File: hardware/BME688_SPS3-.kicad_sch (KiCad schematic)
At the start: 6 parts, among them U59 USBLC6-2P6, U6 BME688

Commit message: updated annotations
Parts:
- renumbered C25 to C501, C12 to C502, D11 to D501, SPS30_Connector4 to SPS30_Connector501, U6 to U501, U59 to U502
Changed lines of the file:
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@@
 		(dnp no)
 		(fields_autoplaced yes)
-		(property "Reference" "#PWR026"
+		(property "Reference" "#PWR0502"
 			(at 121.92 132.08 0)
 			(effects
@@
 			(project "Senior_Design"
 				(path "/8f5928e8-0fc1-4443-a20f-3bfeb956761e/140ad835-eaa4-4a8c-a4e7-0525bbf22a2e"
-					(reference "#PWR026")
+					(reference "#PWR0502")
 					(unit 1)
 				)
@@
 		(dnp no)
 		(fields_autoplaced yes)
-		(property "Reference" "#PWR077"
+		(property "Reference" "#PWR0501"
 			(at 87.63 111.76 0)
 			(effects
@@
 			(project "Senior_Design"
 				(path "/8f5928e8-0fc1-4443-a20f-3bfeb956761e/140ad835-eaa4-4a8c-a4e7-0525bbf22a2e"
-					(reference "#PWR077")
+					(reference "#PWR0501")
 					(unit 1)
 				)
@@
 		(on_board yes)
 		(dnp no)
-		(property "Reference" "C12"
+		(property "Reference" "C502"
 			(at 136.398 119.888 0)
 			(effects
@@
 			(project "Senior_Design"
 				(path "/8f5928e8-0fc1-4443-a20f-3bfeb956761e/140ad835-eaa4-4a8c-a4e7-0525bbf22a2e"
-					(reference "C12")
+					(reference "C502")
 					(unit 1)
 				)
@@
 		(dnp no)
 		(fields_autoplaced yes)
-		(property "Reference" "U59"
+		(property "Reference" "U502"
 			(at 141.3511 60.96 0)
 			(effects
@@
 			(project "Senior_Design"
 				(path "/8f5928e8-0fc1-4443-a20f-3bfeb956761e/140ad835-eaa4-4a8c-a4e7-0525bbf22a2e"
-					(reference "U59")
+					(reference "U502")
 					(unit 1)
 				)
@@
 		(dnp no)
 		(fields_autoplaced yes)
-		(property "Reference" "#PWR078"
+		(property "Reference" "#PWR0503"
 			(at 139.7 67.31 0)
 			(effects
@@
 			(project "Senior_Design"
 				(path "/8f5928e8-0fc1-4443-a20f-3bfeb956761e/140ad835-eaa4-4a8c-a4e7-0525bbf22a2e"
-					(reference "#PWR078")
+					(reference "#PWR0503")
 					(unit 1)
 				)
@@
 		(dnp no)
 		(fields_autoplaced yes)
-		(property "Reference" "U6"
+		(property "Reference" "U501"
 			(at 102.87 96.52 0)
 			(effects
@@
 			(project "Senior_Design"
 				(path "/8f5928e8-0fc1-4443-a20f-3bfeb956761e/140ad835-eaa4-4a8c-a4e7-0525bbf22a2e"
-					(reference "U6")
+					(reference "U501")
 					(unit 1)
 				)
@@
 		(dnp no)
 		(fields_autoplaced yes)
-		(property "Reference" "SPS30_Connector4"
+		(property "Reference" "SPS30_Connector501"
 			(at 200.66 113.0299 0)
 			(effects
@@
 			(project "Senior_Design"
 				(path "/8f5928e8-0fc1-4443-a20f-3bfeb956761e/140ad835-eaa4-4a8c-a4e7-0525bbf22a2e"
-					(reference "SPS30_Connector4")
+					(reference "SPS30_Connector501")
 					(unit 1)
 				)
@@
 		(on_board yes)
 		(dnp no)
-		(property "Reference" "C25"
+		(property "Reference" "C501"
 			(at 130.302 116.332 0)
 			(effects
@@
 			(project "Senior_Design"
 				(path "/8f5928e8-0fc1-4443-a20f-3bfeb956761e/140ad835-eaa4-4a8c-a4e7-0525bbf22a2e"
-					(reference "C25")
+					(reference "C501")
 					(unit 1)
 				)
@@
 		(dnp no)
 		(fields_autoplaced yes)
-		(property "Reference" "#FLG0105"
+		(property "Reference" "#FLG0502"
 			(at 137.795 104.14 0)
 			(effects
@@
 			(project "Senior_Design"
 				(path "/8f5928e8-0fc1-4443-a20f-3bfeb956761e/140ad835-eaa4-4a8c-a4e7-0525bbf22a2e"
-					(reference "#FLG0105")
+					(reference "#FLG0502")
 					(unit 1)
 				)
@@
 		(dnp no)
 		(fields_autoplaced yes)
-		(property "Reference" "#FLG0104"
+		(property "Reference" "#FLG0501"
 			(at 132.715 109.22 0)
 			(effects
@@
 			(project "Senior_Design"
 				(path "/8f5928e8-0fc1-4443-a20f-3bfeb956761e/140ad835-eaa4-4a8c-a4e7-0525bbf22a2e"
-					(reference "#FLG0104")
+					(reference "#FLG0501")
 					(unit 1)
 				)
@@
 		(dnp no)
 		(fields_autoplaced yes)
-		(property "Reference" "#PWR0105"
+		(property "Reference" "#PWR0506"
 			(at 190.5 130.81 0)
 			(effects
@@
 			(project "Senior_Design"
 				(path "/8f5928e8-0fc1-4443-a20f-3bfeb956761e/140ad835-eaa4-4a8c-a4e7-0525bbf22a2e"
-					(reference "#PWR0105")
+					(reference "#PWR0506")
 					(unit 1)
 				)
@@
 		(on_board yes)
 		(dnp no)
-		(property "Reference" "D11"
+		(property "Reference" "D501"
 			(at 196.596 98.044 0)
 			(effects
@@
 			(project "Senior_Design"
 				(path "/8f5928e8-0fc1-4443-a20f-3bfeb956761e/140ad835-eaa4-4a8c-a4e7-0525bbf22a2e"
-					(reference "D11")
+					(reference "D501")
 					(unit 1)
 				)
@@
 		(dnp no)
 		(fields_autoplaced yes)
-		(property "Reference" "#PWR092"
+		(property "Reference" "#PWR0505"
 			(at 190.5 97.79 0)
 			(effects
@@
 			(project "Senior_Design"
 				(path "/8f5928e8-0fc1-4443-a20f-3bfeb956761e/140ad835-eaa4-4a8c-a4e7-0525bbf22a2e"
-					(reference "#PWR092")
+					(reference "#PWR0505")
 					(unit 1)
 				)
@@
 		(on_board yes)
 		(dnp no)
-		(property "Reference" "#PWR0116"
+		(property "Reference" "#PWR0507"
 			(at 200.66 107.95 0)
 			(effects
@@
 			(project "Senior_Design"
 				(path "/8f5928e8-0fc1-4443-a20f-3bfeb956761e/140ad835-eaa4-4a8c-a4e7-0525bbf22a2e"
-					(reference "#PWR0116")
+					(reference "#PWR0507")
 					(unit 1)
 				)
@@
 		(dnp no)
 		(fields_autoplaced yes)
-		(property "Reference" "#PWR0114"
+		(property "Reference" "#PWR0504"
 			(at 139.7 82.55 0)
 			(effects
@@
 			(project "Senior_Design"
 				(path "/8f5928e8-0fc1-4443-a20f-3bfeb956761e/140ad835-eaa4-4a8c-a4e7-0525bbf22a2e"
-					(reference "#PWR0114")
-					(unit 1)
-				)
+					(reference "#PWR0504")
+					(unit 1)
+				)

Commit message: footprint update
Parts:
- C501, C502: footprint Capacitor_SMD:C_0402_1005Metric -> Capacitor_SMD:C_0805_2012Metric
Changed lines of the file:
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@@
 			)
 		)
-		(property "Footprint" "Capacitor_SMD:C_0402_1005Metric"
+		(property "Footprint" "Capacitor_SMD:C_0805_2012Metric"
 			(at 135.89 118.11 0)
 			(effects
@@
 			)
 		)
-		(property "Footprint" "Capacitor_SMD:C_0402_1005Metric"
+		(property "Footprint" "Capacitor_SMD:C_0805_2012Metric"
 			(at 130.81 118.11 0)
 			(effects

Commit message: footprint update 2
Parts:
- D501: footprint Package_TO_SOT_THT:TO-220-2_Vertical -> Diode_SMD:D_SOD-123
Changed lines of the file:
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@@
 			)
 		)
-		(property "Footprint" "Package_TO_SOT_THT:TO-220-2_Vertical"
+		(property "Footprint" "Diode_SMD:D_SOD-123"
 			(at 194.31 106.045 0)
 			(effects

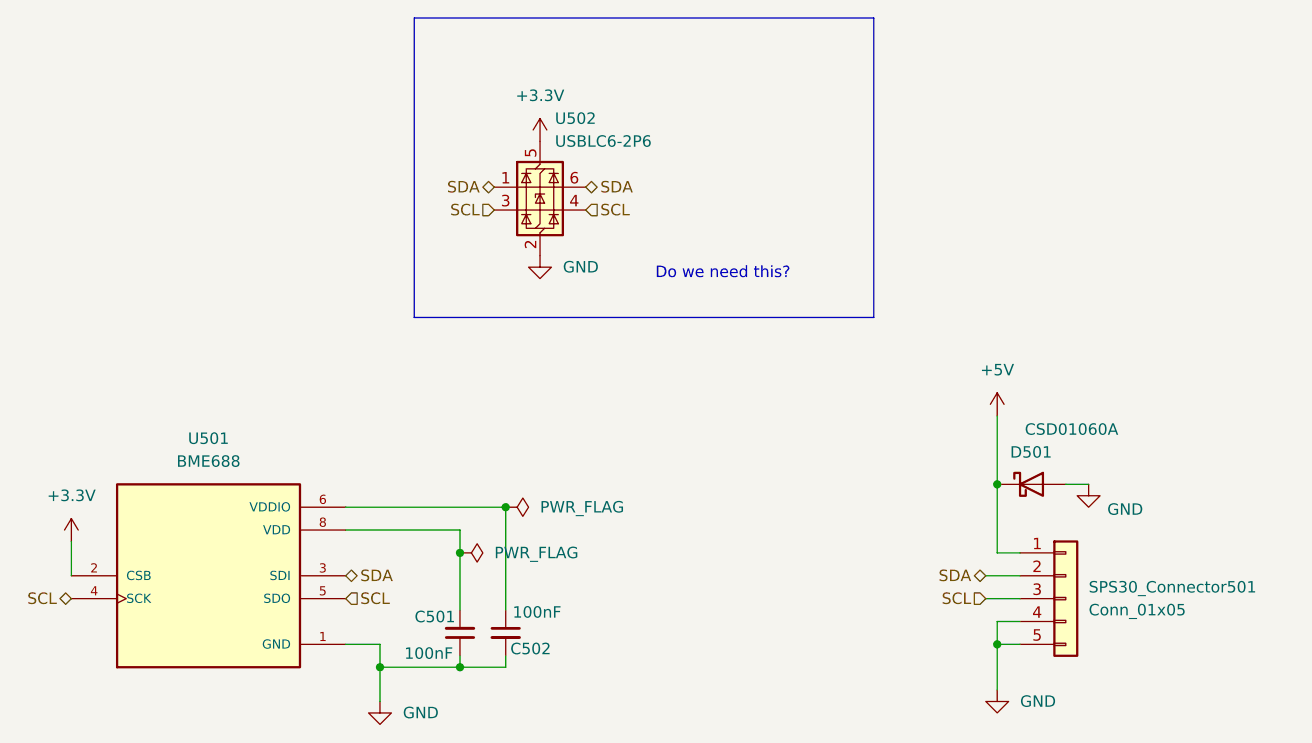
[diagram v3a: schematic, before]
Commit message: updated ESD/Inductor footprints
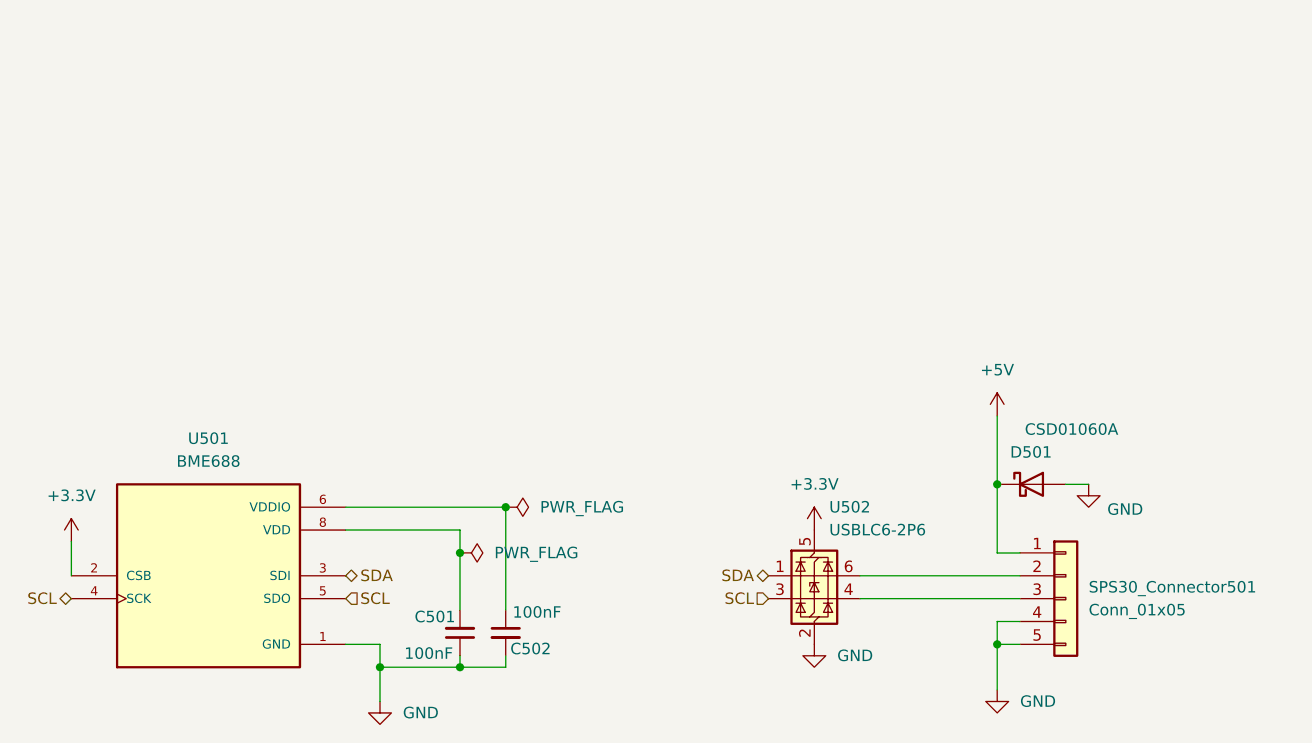
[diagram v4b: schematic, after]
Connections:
- net SCL: no longer SPS30_Connector501.3 (Pin_3), U502.4 (I/O2)
- net SDA: no longer SPS30_Connector501.2 (Pin_2), U502.6 (I/O1)
- new net: SPS30_Connector501.3 (Pin_3), U502.4 (I/O2)
- new net: SPS30_Connector501.2 (Pin_2), U502.6 (I/O1)
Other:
- note removed: "Do we need this?"
- moved on the sheet: U502
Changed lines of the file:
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@@
 	(generator_version "9.0")
 	(paper "A4")
-	(rectangle
-		(start 125.73 49.784)
-		(end 176.784 83.058)
-		(stroke
-			(width 0)
-			(type default)
-		)
-		(fill
-			(type none)
-		)
-	)
-	(text "Do we need this?"
-		(exclude_from_sim no)
-		(at 160.02 78.232 0)
-		(effects
-			(font
-				(size 1.27 1.27)
-				(color 255 0 0 1)
-			)
-		)
-	)
 	(junction
 		(at 135.89 104.14)
@@
 	(wire
 		(pts
-			(xy 189.23 111.76) (xy 193.04 111.76)
-		)
-		(stroke
-			(width 0)
-			(type default)
-		)
-	)
-	(wire
-		(pts
 			(xy 198.12 101.6) (xy 200.66 101.6)
 		)
@@
 	(wire
 		(pts
+			(xy 175.26 114.3) (xy 193.04 114.3)
+		)
+		(stroke
+			(width 0)
+			(type default)
+		)
+	)
+	(wire
+		(pts
 			(xy 135.89 120.65) (xy 135.89 121.92)
 		)
@@
 	(wire
 		(pts
-			(xy 189.23 114.3) (xy 193.04 114.3)
-		)
-		(stroke
-			(width 0)
-			(type default)
-		)
-	)
-	(wire
-		(pts
 			(xy 130.81 106.68) (xy 130.81 109.22)
+		)
+		(stroke
+			(width 0)
+			(type default)
+		)
+	)
+	(wire
+		(pts
+			(xy 175.26 111.76) (xy 193.04 111.76)
 		)
 		(stroke
@@
 	(hierarchical_label "SDA"
 		(shape bidirectional)
-		(at 134.62 68.58 180)
+		(at 165.1 111.76 180)
 		(effects
 			(font
@@
 	(hierarchical_label "SCL"
 		(shape input)
-		(at 134.62 71.12 180)
+		(at 165.1 114.3 180)
 		(effects
 			(font
@@
 			)
 			(justify right)
-		)
-	)
-	(hierarchical_label "SDA"
-		(shape bidirectional)
-		(at 189.23 111.76 180)
-		(effects
-			(font
-				(size 1.27 1.27)
-			)
-			(justify right)
-		)
-	)
-	(hierarchical_label "SCL"
-		(shape input)
-		(at 189.23 114.3 180)
-		(effects
-			(font
-				(size 1.27 1.27)
-			)
-			(justify right)
-		)
-	)
-	(hierarchical_label "SDA"
-		(shape bidirectional)
-		(at 144.78 68.58 0)
-		(effects
-			(font
-				(size 1.27 1.27)
-			)
-			(justify left)
-		)
-	)
-	(hierarchical_label "SCL"
-		(shape input)
-		(at 144.78 71.12 0)
-		(effects
-			(font
-				(size 1.27 1.27)
-			)
-			(justify left)
 		)
 	)
@@
 	(symbol
 		(lib_id "Power_Protection:USBLC6-2P6")
-		(at 139.7 68.58 0)
+		(at 170.18 111.76 0)
 		(unit 1)
 		(exclude_from_sim no)
@@
 		(fields_autoplaced yes)
 		(property "Reference" "U502"
-			(at 141.3511 60.96 0)
+			(at 171.8311 104.14 0)
 			(effects
 				(font
@@
 		)
 		(property "Value" "USBLC6-2P6"
-			(at 141.3511 63.5 0)
+			(at 171.8311 106.68 0)
 			(effects
 				(font
@@
 		)
 		(property "Footprint" "Package_TO_SOT_SMD:SOT-666"
-			(at 140.716 75.311 0)
+			(at 171.196 118.491 0)
 			(effects
 				(font
@@
 		)
 		(property "Datasheet" "https://www.st.com/resource/en/datasheet/usblc6-2.pdf"
-			(at 140.716 77.216 0)
+			(at 171.196 120.396 0)
 			(effects
 				(font
@@
 		)
 		(property "Description" "Very low capacitance ESD protection diode, 2 data-line, SOT-666"
-			(at 139.7 68.58 0)
+			(at 170.18 111.76 0)
 			(effects
 				(font
@@
 	(symbol
 		(lib_id "power:+3.3V")
-		(at 139.7 63.5 0)
+		(at 170.18 106.68 0)
 		(unit 1)
 		(exclude_from_sim no)
@@
 		(fields_autoplaced yes)
 		(property "Reference" "#PWR0503"
-			(at 139.7 67.31 0)
+			(at 170.18 110.49 0)
 			(effects
 				(font
@@
 		)
 		(property "Value" "+3.3V"
-			(at 139.7 58.42 0)
+			(at 170.18 101.6 0)
 			(effects
 				(font
@@
 		)
 		(property "Footprint" ""
-			(at 139.7 63.5 0)
+			(at 170.18 106.68 0)
 			(effects
 				(font
@@
 		)
 		(property "Datasheet" ""
-			(at 139.7 63.5 0)
+			(at 170.18 106.68 0)
 			(effects
 				(font
@@
 		)
 		(property "Description" "Power symbol creates a global label with name \"+3.3V\""
-			(at 139.7 63.5 0)
+			(at 170.18 106.68 0)
 			(effects
 				(font
@@
 	(symbol
 		(lib_id "power:GND")
-		(at 139.7 76.2 0)
+		(at 170.18 119.38 0)
 		(unit 1)
 		(exclude_from_sim no)
@@
 		(fields_autoplaced yes)
 		(property "Reference" "#PWR0504"
-			(at 139.7 82.55 0)
+			(at 170.18 125.73 0)
 			(effects
 				(font
@@
 		)
 		(property "Value" "GND"
-			(at 142.24 77.4699 0)
+			(at 172.72 120.6499 0)
 			(effects
 				(font
@@
 		)
 		(property "Footprint" ""
-			(at 139.7 76.2 0)
+			(at 170.18 119.38 0)
 			(effects
 				(font
@@
 		)
 		(property "Datasheet" ""
-			(at 139.7 76.2 0)
+			(at 170.18 119.38 0)
 			(effects
 				(font
@@
 		)
 		(property "Description" "Power symbol creates a global label with name \"GND\" , ground"
-			(at 139.7 76.2 0)
-			(effects
-				(font
+			(at 170.18 119.38 0)
+			(effects
+				(font

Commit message: updated footprints
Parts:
- SPS30_Connector501: footprint Connector_PinHeader_2.54mm:PinHeader_1x05_P2.54mm_Vertical -> Connector_JST:JST_ZH_B5B-ZR_1x05_P1.50mm_Vertical
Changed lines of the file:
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@@
 			)
 		)
-		(property "Footprint" "Connector_PinHeader_2.54mm:PinHeader_1x05_P2.54mm_Vertical"
+		(property "Footprint" "Connector_JST:JST_ZH_B5B-ZR_1x05_P1.50mm_Vertical"
 			(at 198.12 114.3 0)
 			(effects

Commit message: reannotate
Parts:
- renumbered C501 to C401, C502 to C402, D501 to D401, SPS30_Connector501 to SPS30_Connector401, U501 to U401, U502 to U402
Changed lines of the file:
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@@
 		(dnp no)
 		(fields_autoplaced yes)
-		(property "Reference" "#PWR0507"
+		(property "Reference" "#PWR0407"
 			(at 121.92 132.08 0)
 			(effects
@@
 			(project "Senior_Design"
 				(path "/8f5928e8-0fc1-4443-a20f-3bfeb956761e/140ad835-eaa4-4a8c-a4e7-0525bbf22a2e"
-					(reference "#PWR0507")
+					(reference "#PWR0407")
 					(unit 1)
 				)
@@
 		(dnp no)
 		(fields_autoplaced yes)
-		(property "Reference" "#PWR0504"
+		(property "Reference" "#PWR0404"
 			(at 87.63 111.76 0)
 			(effects
@@
 			(project "Senior_Design"
 				(path "/8f5928e8-0fc1-4443-a20f-3bfeb956761e/140ad835-eaa4-4a8c-a4e7-0525bbf22a2e"
-					(reference "#PWR0504")
+					(reference "#PWR0404")
 					(unit 1)
 				)
@@
 		(on_board yes)
 		(dnp no)
-		(property "Reference" "C502"
+		(property "Reference" "C402"
 			(at 136.398 119.888 0)
 			(effects
@@
 			(project "Senior_Design"
 				(path "/8f5928e8-0fc1-4443-a20f-3bfeb956761e/140ad835-eaa4-4a8c-a4e7-0525bbf22a2e"
-					(reference "C502")
+					(reference "C402")
 					(unit 1)
 				)
@@
 		(dnp no)
 		(fields_autoplaced yes)
-		(property "Reference" "U502"
+		(property "Reference" "U402"
 			(at 171.8311 104.14 0)
 			(effects
@@
 			(project "Senior_Design"
 				(path "/8f5928e8-0fc1-4443-a20f-3bfeb956761e/140ad835-eaa4-4a8c-a4e7-0525bbf22a2e"
-					(reference "U502")
+					(reference "U402")
 					(unit 1)
 				)
@@
 		(dnp no)
 		(fields_autoplaced yes)
-		(property "Reference" "#PWR0503"
+		(property "Reference" "#PWR0403"
 			(at 170.18 110.49 0)
 			(effects
@@
 			(project "Senior_Design"
 				(path "/8f5928e8-0fc1-4443-a20f-3bfeb956761e/140ad835-eaa4-4a8c-a4e7-0525bbf22a2e"
-					(reference "#PWR0503")
+					(reference "#PWR0403")
 					(unit 1)
 				)
@@
 		(dnp no)
 		(fields_autoplaced yes)
-		(property "Reference" "U501"
+		(property "Reference" "U401"
 			(at 102.87 96.52 0)
 			(effects
@@
 			(project "Senior_Design"
 				(path "/8f5928e8-0fc1-4443-a20f-3bfeb956761e/140ad835-eaa4-4a8c-a4e7-0525bbf22a2e"
-					(reference "U501")
+					(reference "U401")
 					(unit 1)
 				)
@@
 		(dnp no)
 		(fields_autoplaced yes)
-		(property "Reference" "SPS30_Connector501"
+		(property "Reference" "SPS30_Connector401"
 			(at 200.66 113.0299 0)
 			(effects
@@
 			(project "Senior_Design"
 				(path "/8f5928e8-0fc1-4443-a20f-3bfeb956761e/140ad835-eaa4-4a8c-a4e7-0525bbf22a2e"
-					(reference "SPS30_Connector501")
+					(reference "SPS30_Connector401")
 					(unit 1)
 				)
@@
 		(on_board yes)
 		(dnp no)
-		(property "Reference" "C501"
+		(property "Reference" "C401"
 			(at 130.302 116.332 0)
 			(effects
@@
 			(project "Senior_Design"
 				(path "/8f5928e8-0fc1-4443-a20f-3bfeb956761e/140ad835-eaa4-4a8c-a4e7-0525bbf22a2e"
-					(reference "C501")
+					(reference "C401")
 					(unit 1)
 				)
@@
 		(dnp no)
 		(fields_autoplaced yes)
-		(property "Reference" "#FLG0501"
+		(property "Reference" "#FLG0401"
 			(at 137.795 104.14 0)
 			(effects
@@
 			(project "Senior_Design"
 				(path "/8f5928e8-0fc1-4443-a20f-3bfeb956761e/140ad835-eaa4-4a8c-a4e7-0525bbf22a2e"
-					(reference "#FLG0501")
+					(reference "#FLG0401")
 					(unit 1)
 				)
@@
 		(dnp no)
 		(fields_autoplaced yes)
-		(property "Reference" "#FLG0502"
+		(property "Reference" "#FLG0402"
 			(at 132.715 109.22 0)
 			(effects
@@
 			(project "Senior_Design"
 				(path "/8f5928e8-0fc1-4443-a20f-3bfeb956761e/140ad835-eaa4-4a8c-a4e7-0525bbf22a2e"
-					(reference "#FLG0502")
+					(reference "#FLG0402")
 					(unit 1)
 				)
@@
 		(dnp no)
 		(fields_autoplaced yes)
-		(property "Reference" "#PWR0506"
+		(property "Reference" "#PWR0406"
 			(at 190.5 130.81 0)
 			(effects
@@
 			(project "Senior_Design"
 				(path "/8f5928e8-0fc1-4443-a20f-3bfeb956761e/140ad835-eaa4-4a8c-a4e7-0525bbf22a2e"
-					(reference "#PWR0506")
+					(reference "#PWR0406")
 					(unit 1)
 				)
@@
 		(on_board yes)
 		(dnp no)
-		(property "Reference" "D501"
+		(property "Reference" "D401"
 			(at 196.596 98.044 0)
 			(effects
@@
 			(project "Senior_Design"
 				(path "/8f5928e8-0fc1-4443-a20f-3bfeb956761e/140ad835-eaa4-4a8c-a4e7-0525bbf22a2e"
-					(reference "D501")
+					(reference "D401")
 					(unit 1)
 				)
@@
 		(dnp no)
 		(fields_autoplaced yes)
-		(property "Reference" "#PWR0501"
+		(property "Reference" "#PWR0401"
 			(at 190.5 97.79 0)
 			(effects
@@
 			(project "Senior_Design"
 				(path "/8f5928e8-0fc1-4443-a20f-3bfeb956761e/140ad835-eaa4-4a8c-a4e7-0525bbf22a2e"
-					(reference "#PWR0501")
+					(reference "#PWR0401")
 					(unit 1)
 				)
@@
 		(on_board yes)
 		(dnp no)
-		(property "Reference" "#PWR0502"
+		(property "Reference" "#PWR0402"
 			(at 200.66 107.95 0)
 			(effects
@@
 			(project "Senior_Design"
 				(path "/8f5928e8-0fc1-4443-a20f-3bfeb956761e/140ad835-eaa4-4a8c-a4e7-0525bbf22a2e"
-					(reference "#PWR0502")
+					(reference "#PWR0402")
 					(unit 1)
 				)
@@
 		(dnp no)
 		(fields_autoplaced yes)
-		(property "Reference" "#PWR0505"
+		(property "Reference" "#PWR0405"
 			(at 170.18 125.73 0)
 			(effects
@@
 			(project "Senior_Design"
 				(path "/8f5928e8-0fc1-4443-a20f-3bfeb956761e/140ad835-eaa4-4a8c-a4e7-0525bbf22a2e"
-					(reference "#PWR0505")
-					(unit 1)
-				)
+					(reference "#PWR0405")
+					(unit 1)
+				)
